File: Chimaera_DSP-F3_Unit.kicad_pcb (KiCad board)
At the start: 2 copper layers, 80 x 44 mm, 87 parts, among them J1 USB_MINI, J51 RJ45-TRANSFO, P1 power in, P11 CONN_6, P2 from sensor units, P3 from sensor units, P5 to sensor units, SW1 DPDT, U1 LM1117, U2 MCP1703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

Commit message: bug-fix in DSP with wrongly wired I2C2
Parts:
- added G***: OSHW_LOGO, OSHW_LOGO, F.Cu at (18.5, 27.8)
- added P12: CONN_2, SIL-2, F.Cu at (54.0, 51.8)
- U4: value F303Cx -> STM32F303CX
- moved R7 23.0 mm to (75.5, 45.8), turned to 270 degrees
- moved D1 5.67 mm to (77.8, 49.0), turned to 270 degrees
- moved C21 3.75 mm to (67.5, 50.5)
- moved C23 3.75 mm to (58.5, 50.5)
- moved R6 3.75 mm to (55.5, 48.2)
- moved U5 3.75 mm to (70.2, 47.0)
- moved U7 3.75 mm to (61.2, 47.0)
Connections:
- P11 pad 5: N-0000010 -> SCL
- P11 pad 6: N-000009 -> SDA
- U4 pad 21: SCL -> N-0000022
- U4 pad 22: SDA -> N-0000026
- U4 pad 30: N-0000010 -> SCL
- U4 pad 31: N-000009 -> SDA
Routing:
- net SCL: track 27.1 -> 51.3 mm
- net N-000009: track 22.3 -> 0.00 mm
- net N-0000010: track 20.1 -> 0.00 mm
- net SDA: track 26.4 -> 45.4 mm
- net N-0000026: track 0.00 -> 14.9 mm
- net N-0000022: track 0.00 -> 13.2 mm
- net +3.3V: track 322.1 -> 313.5 mm
- net GND: track 201.3 -> 194.8 mm, vias 67 -> 65
- net N-0000042: track 134.8 -> 133.2 mm
- net BOOT0: track 54.6 -> 54.7 mm, vias 2 -> 6
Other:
- board text added: "I2C2 USART1"
- board text added: "RX SDA"
- board text added: "TX SCL"
- board text added: "USART3"
- board text removed: "USART1"

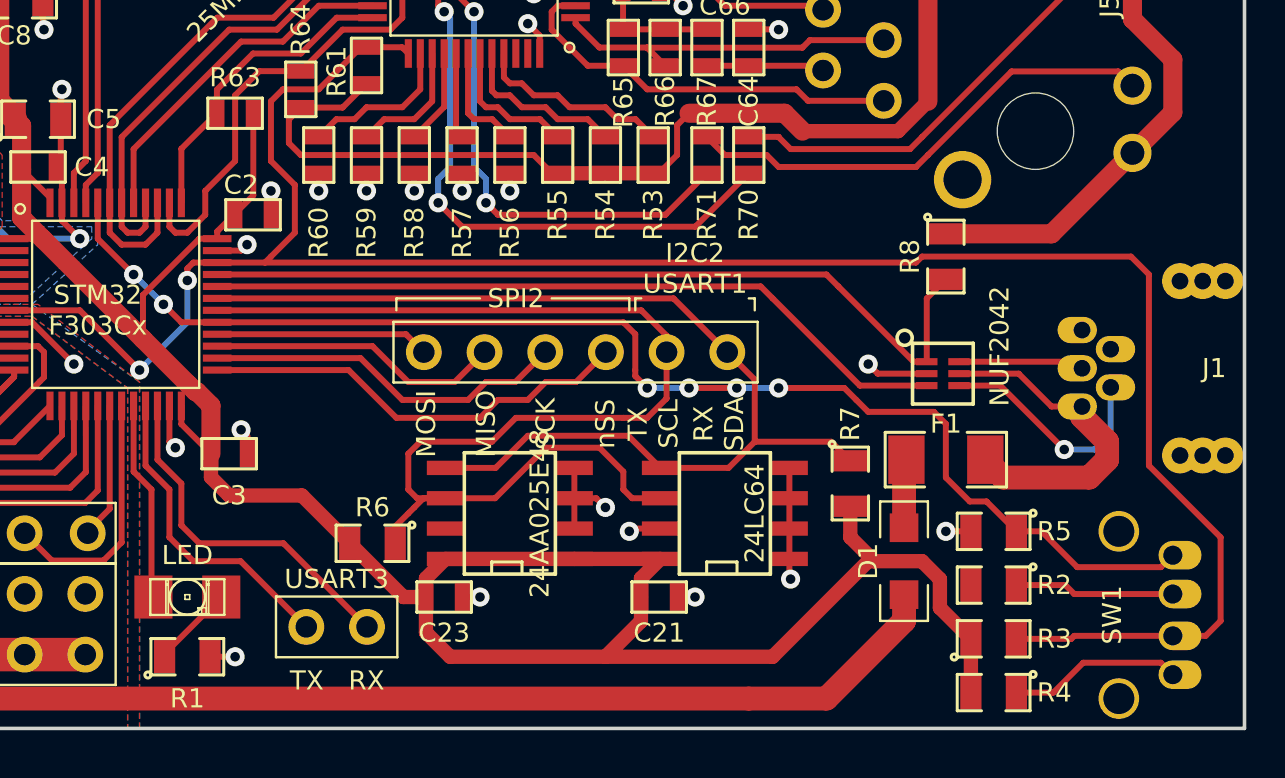
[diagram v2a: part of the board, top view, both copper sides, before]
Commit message: EDA: all resistors now in 0603 format
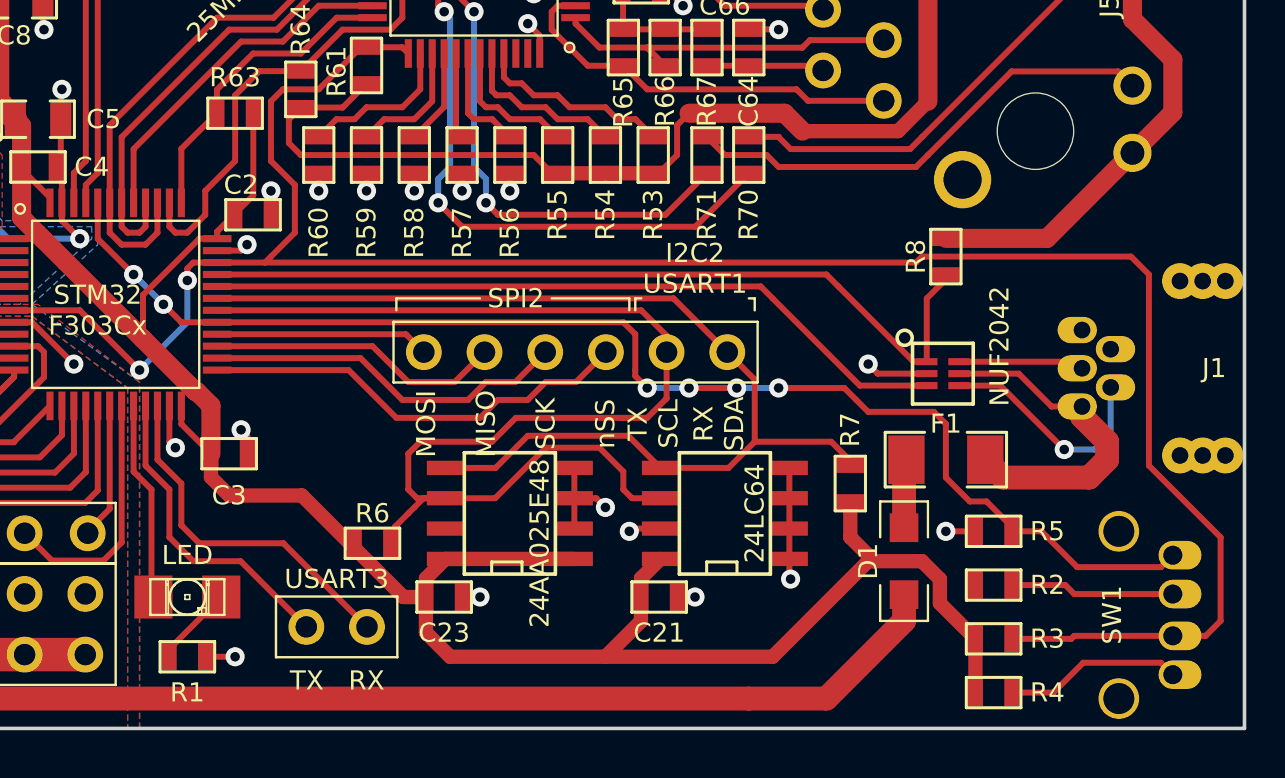
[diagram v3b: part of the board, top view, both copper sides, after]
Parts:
- R1, R2, R3, R4, R5, R6, R7, R8: footprint SM0805 -> SM0603
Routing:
- net +3.3V: track 313.5 -> 310.0 mm

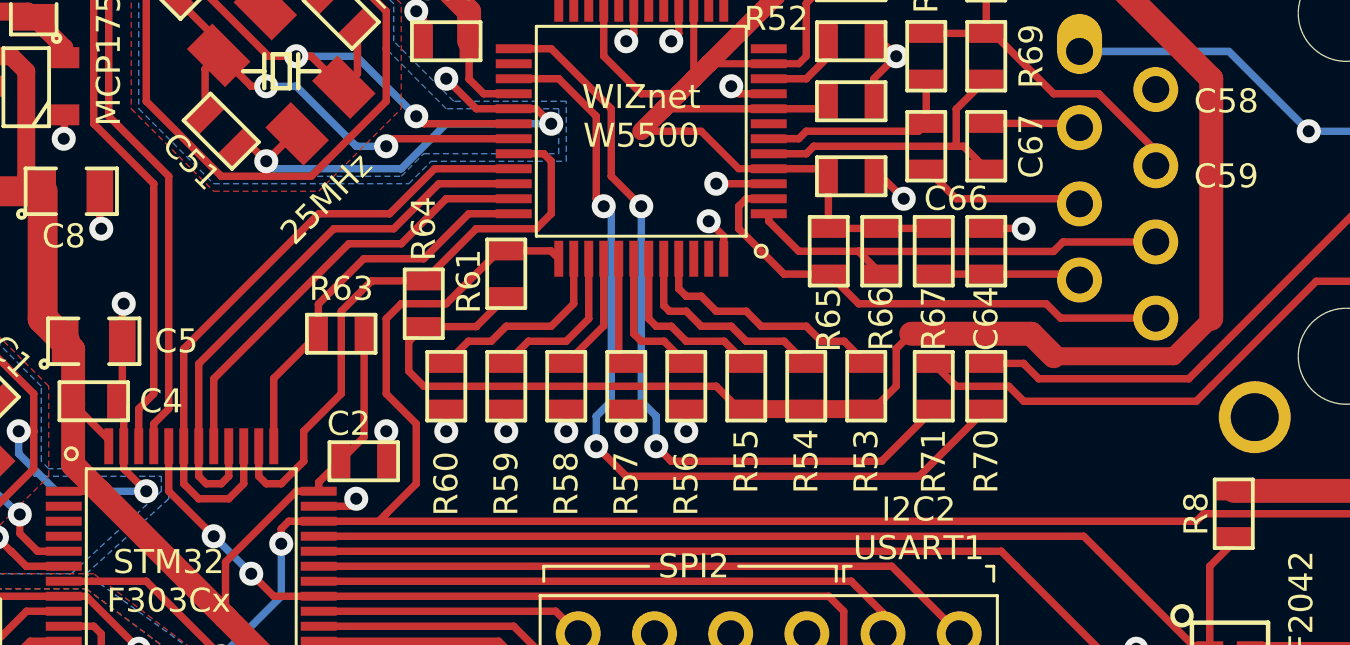
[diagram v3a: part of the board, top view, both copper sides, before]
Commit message: equal length traces for differential ethernet lanes
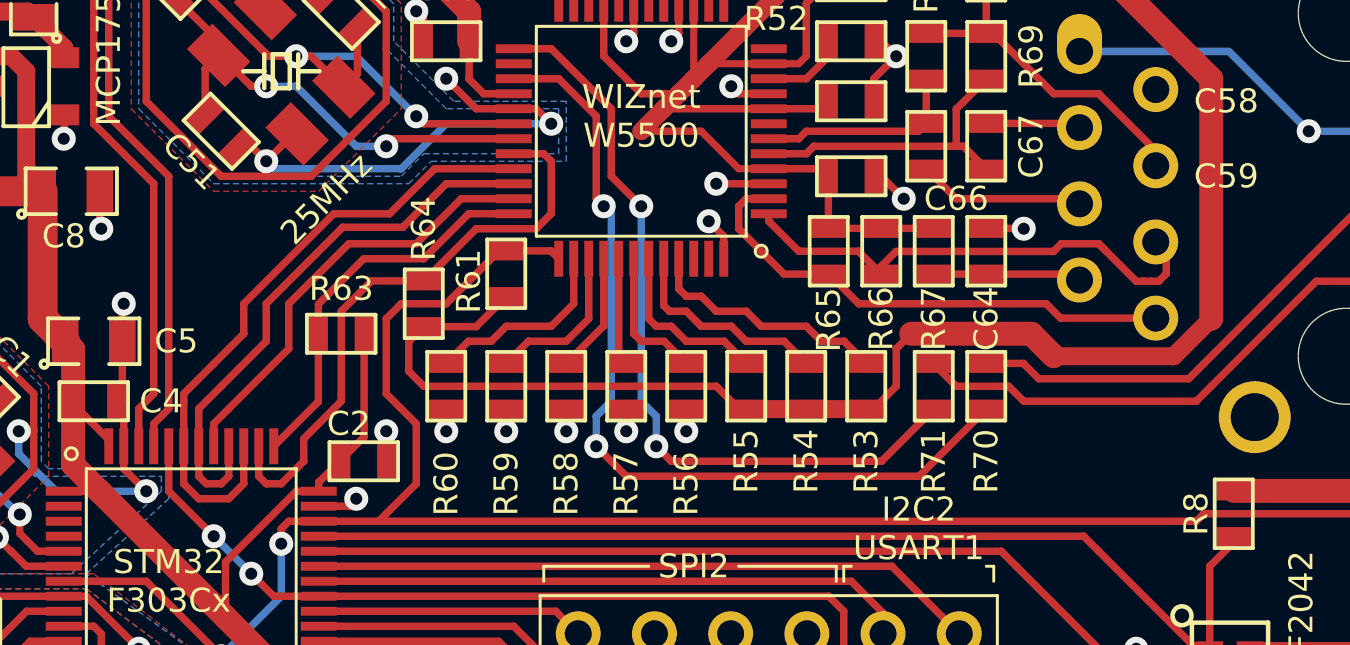
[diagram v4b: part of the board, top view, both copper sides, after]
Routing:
- net TXN: track 14.8 -> 17.0 mm
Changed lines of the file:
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@@
     (thickness 1.6)
     (drawings 36)
-    (tracks 1032)
+    (tracks 1057)
     (zones 0)
     (modules 89)
@@
     (18 B.Paste user)
     (19 F.Paste user)
-    (20 B.SilkS user hide)
+    (20 B.SilkS user)
     (21 F.SilkS user)
     (22 B.Mask user)
@@
     (pcbplotparams
       (layerselection 284196865)
-      (usegerberextensions true)
+      (usegerberextensions false)
       (excludeedgelayer false)
       (linewidth 0.150000)
@@
       (padsonsilk false)
       (subtractmaskfromsilk false)
-      (outputformat 1)
+      (outputformat 3)
       (mirror false)
-      (drillshape 0)
+      (drillshape 2)
       (scaleselection 1)
       (outputdirectory ../gerber/DSP-F3_Unit/rev4/))
@@
   (segment (start 25.7 52.91) (end 28.24 52.91) (width 1.4) (layer F.Cu) (net 5) (status 30))
   (segment (start 23.16 52.91) (end 25.7 52.91) (width 1.4) (layer F.Cu) (net 5) (status 30))
-  (segment (start 45 34) (end 45 31.25) (width 0.25) (layer F.Cu) (net 6))
-  (segment (start 53 25.25) (end 55.5 25.25) (width 0.25) (layer F.Cu) (net 6))
-  (segment (start 51.5 26.75) (end 53 25.25) (width 0.25) (layer F.Cu) (net 6))
-  (segment (start 49.5 26.75) (end 51.5 26.75) (width 0.25) (layer F.Cu) (net 6))
-  (segment (start 45 31.25) (end 49.5 26.75) (width 0.25) (layer F.Cu) (net 6))
+  (segment (start 45 32.75) (end 45.75 32) (width 0.25) (layer F.Cu) (net 6))
+  (segment (start 47.25 29.25) (end 49.799998 26.700002) (width 0.25) (layer F.Cu) (net 6))
+  (segment (start 47.25 30.5) (end 47.25 29.25) (width 0.25) (layer F.Cu) (net 6))
+  (segment (start 45.75 32) (end 47.25 30.5) (width 0.25) (layer F.Cu) (net 6))
+  (segment (start 45.75 32) (end 45.75 32) (width 0.25) (layer F.Cu) (net 6))
+  (segment (start 45 34) (end 45 32.75) (width 0.25) (layer F.Cu) (net 6))
+  (segment (start 53.25 25.25) (end 55.5 25.25) (width 0.25) (layer F.Cu) (net 6))
+  (segment (start 51.799998 26.700002) (end 53.25 25.25) (width 0.25) (layer F.Cu) (net 6))
+  (segment (start 49.799998 26.700002) (end 51.799998 26.700002) (width 0.25) (layer F.Cu) (net 6))
   (segment (start 46 34) (end 46 35) (width 0.25) (layer F.Cu) (net 6))
   (segment (start 45 35) (end 45 34) (width 0.25) (layer F.Cu) (net 6))
@@
   (segment (start 45.75 35.25) (end 45.25 35.25) (width 0.25) (layer F.Cu) (net 6))
   (segment (start 46 35) (end 45.75 35.25) (width 0.25) (layer F.Cu) (net 6))
-  (segment (start 55.5 25.75) (end 53.25 25.75) (width 0.25) (layer F.Cu) (net 7))
-  (segment (start 45.5 31.75) (end 45.5 34) (width 0.25) (layer F.Cu) (net 7))
-  (segment (start 50 27.25) (end 45.5 31.75) (width 0.25) (layer F.Cu) (net 7))
-  (segment (start 51.75 27.25) (end 50 27.25) (width 0.25) (layer F.Cu) (net 7))
-  (segment (start 53.25 25.75) (end 51.75 27.25) (width 0.25) (layer F.Cu) (net 7))
-  (segment (start 44.5 34) (end 44.5 30.75) (width 0.25) (layer F.Cu) (net 8))
+  (segment (start 45.5 34) (end 45.5 33.25) (width 0.25) (layer F.Cu) (net 7))
+  (segment (start 48 29.25) (end 50 27.25) (width 0.25) (layer F.Cu) (net 7))
+  (segment (start 48 30.75) (end 48 29.25) (width 0.25) (layer F.Cu) (net 7))
+  (segment (start 46 32.75) (end 48 30.75) (width 0.25) (layer F.Cu) (net 7))
+  (segment (start 46 32.75) (end 46 32.75) (width 0.25) (layer F.Cu) (net 7))
+  (segment (start 45.5 33.25) (end 46 32.75) (width 0.25) (layer F.Cu) (net 7))
+  (segment (start 53.75 25.75) (end 55.5 25.75) (width 0.25) (layer F.Cu) (net 7))
+  (segment (start 52.25 27.25) (end 53.75 25.75) (width 0.25) (layer F.Cu) (net 7))
+  (segment (start 50 27.25) (end 52.25 27.25) (width 0.25) (layer F.Cu) (net 7))
+  (segment (start 44.5 32.5) (end 44.5 32.25) (width 0.25) (layer F.Cu) (net 8))
+  (segment (start 44.5 32.25) (end 45.5 31.25) (width 0.25) (layer F.Cu) (net 8))
+  (segment (start 46.5 29.25) (end 49.5 26.25) (width 0.25) (layer F.Cu) (net 8))
+  (segment (start 46.5 30.25) (end 46.5 29.25) (width 0.25) (layer F.Cu) (net 8))
+  (segment (start 45.5 31.25) (end 46.5 30.25) (width 0.25) (layer F.Cu) (net 8))
+  (segment (start 45.5 31.25) (end 45.5 31.25) (width 0.25) (layer F.Cu) (net 8))
+  (segment (start 44.5 34) (end 44.5 32.5) (width 0.25) (layer F.Cu) (net 8))
   (segment (start 52.863602 24.75) (end 55.5 24.75) (width 0.25) (layer F.Cu) (net 8))
   (segment (start 51.363602 26.25) (end 52.863602 24.75) (width 0.25) (layer F.Cu) (net 8))
-  (segment (start 49 26.25) (end 51.363602 26.25) (width 0.25) (layer F.Cu) (net 8))
-  (segment (start 44.5 30.75) (end 49 26.25) (width 0.25) (layer F.Cu) (net 8))
+  (segment (start 49.5 26.25) (end 51.363602 26.25) (width 0.25) (layer F.Cu) (net 8))
   (segment (start 46.5 34) (end 46.5 35.25) (width 0.25) (layer F.Cu) (net 8))
   (segment (start 44.5 35.25) (end 44.5 34) (width 0.25) (layer F.Cu) (net 8))
@@
   (segment (start 46 35.75) (end 45 35.75) (width 0.25) (layer F.Cu) (net 8))
   (segment (start 46.5 35.25) (end 46 35.75) (width 0.25) (layer F.Cu) (net 8))
-  (segment (start 47.5 34) (end 47.5 31.738) (width 0.25) (layer F.Cu) (net 9))
-  (segment (start 47.5 31.738) (end 48.988 30.25) (width 0.25) (layer F.Cu) (net 9))
+  (segment (start 48.988 30.25) (end 48.988 32.512) (width 0.25) (layer F.Cu) (net 9))
+  (segment (start 48.988 32.512) (end 47.5 34) (width 0.25) (layer F.Cu) (net 9))
   (segment (start 55.5 26.25) (end 54 26.25) (width 0.25) (layer F.Cu) (net 9))
   (segment (start 48.988 29.262) (end 48.988 30.25) (width 0.25) (layer F.Cu) (net 9))
@@
   (segment (start 52.5 27.75) (end 50.5 27.75) (width 0.25) (layer F.Cu) (net 9))
   (segment (start 54 26.25) (end 52.5 27.75) (width 0.25) (layer F.Cu) (net 9))
+  (segment (start 48.5 33.75) (end 49.75 32.5) (width 0.25) (layer F.Cu) (net 10))
+  (segment (start 49.75 32.5) (end 49.75 32.25) (width 0.25) (layer F.Cu) (net 10))
   (segment (start 52.5 28.488) (end 50.762 28.488) (width 0.25) (layer F.Cu) (net 10))
   (segment (start 47 35) (end 47 34) (width 0.25) (layer F.Cu) (net 10))
@@
   (segment (start 47.75 35.25) (end 47.25 35.25) (width 0.25) (layer F.Cu) (net 10))
   (segment (start 48.5 34.5) (end 47.75 35.25) (width 0.25) (layer F.Cu) (net 10))
-  (segment (start 48.5 33.5) (end 48.5 34.5) (width 0.25) (layer F.Cu) (net 10))
-  (segment (start 49.75 32.25) (end 48.5 33.5) (width 0.25) (layer F.Cu) (net 10))
+  (segment (start 48.5 33.75) (end 48.5 34.5) (width 0.25) (layer F.Cu) (net 10))
   (segment (start 49.75 29.5) (end 49.75 32.25) (width 0.25) (layer F.Cu) (net 10))
   (segment (start 50.762 28.488) (end 49.75 29.5) (width 0.25) (layer F.Cu) (net 10))
@@
   (segment (start 74.162 28.262) (end 74.36 28.46) (width 0.25) (layer F.Cu) (net 66))
   (segment (start 69.5 28.262) (end 71.25 28.262) (width 0.25) (layer F.Cu) (net 66))
-  (segment (start 66.994 27.506) (end 73.494 27.506) (width 0.25) (layer F.Cu) (net 67))
-  (segment (start 73.81 27.19) (end 76.9 27.19) (width 0.25) (layer F.Cu) (net 67))
-  (segment (start 73.494 27.506) (end 73.81 27.19) (width 0.25) (layer F.Cu) (net 67))
+  (segment (start 67.75 28.262) (end 67.75 28) (width 0.25) (layer F.Cu) (net 67))
+  (segment (start 68.244 27.506) (end 73.494 27.506) (width 0.25) (layer F.Cu) (net 67))
+  (segment (start 67.75 28) (end 68.244 27.506) (width 0.25) (layer F.Cu) (net 67))
+  (segment (start 77 28.5) (end 77.25 28.25) (width 0.25) (layer F.Cu) (net 67))
+  (segment (start 77.25 27.54) (end 76.9 27.19) (width 0.25) (layer F.Cu) (net 67))
+  (segment (start 77.25 28.25) (end 77.25 27.54) (width 0.25) (layer F.Cu) (net 67))
+  (segment (start 76.5 28.5) (end 76.75 28.5) (width 0.25) (layer F.Cu) (net 67))
+  (segment (start 76.75 28.5) (end 77 28.5) (width 0.25) (layer F.Cu) (net 67))
+  (segment (start 73.75 27.25) (end 75 27.25) (width 0.25) (layer F.Cu) (net 67))
+  (segment (start 75 27.25) (end 75.25 27.5) (width 0.25) (layer F.Cu) (net 67))
+  (segment (start 76.25 28.5) (end 76.5 28.5) (width 0.25) (layer F.Cu) (net 67))
+  (segment (start 75 27.25) (end 75.25 27.5) (width 0.25) (layer F.Cu) (net 67))
+  (segment (start 75.25 27.5) (end 76.25 28.5) (width 0.25) (layer F.Cu) (net 67))
+  (segment (start 73.494 27.506) (end 73.75 27.25) (width 0.25) (layer F.Cu) (net 67))
   (segment (start 64 26.25) (end 64 26.5) (width 0.25) (layer F.Cu) (net 67))
   (segment (start 66.988 27.5) (end 66.994 27.506) (width 0.25) (layer F.Cu) (net 67))
